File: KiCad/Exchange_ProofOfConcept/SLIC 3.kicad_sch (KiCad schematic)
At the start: 9 parts

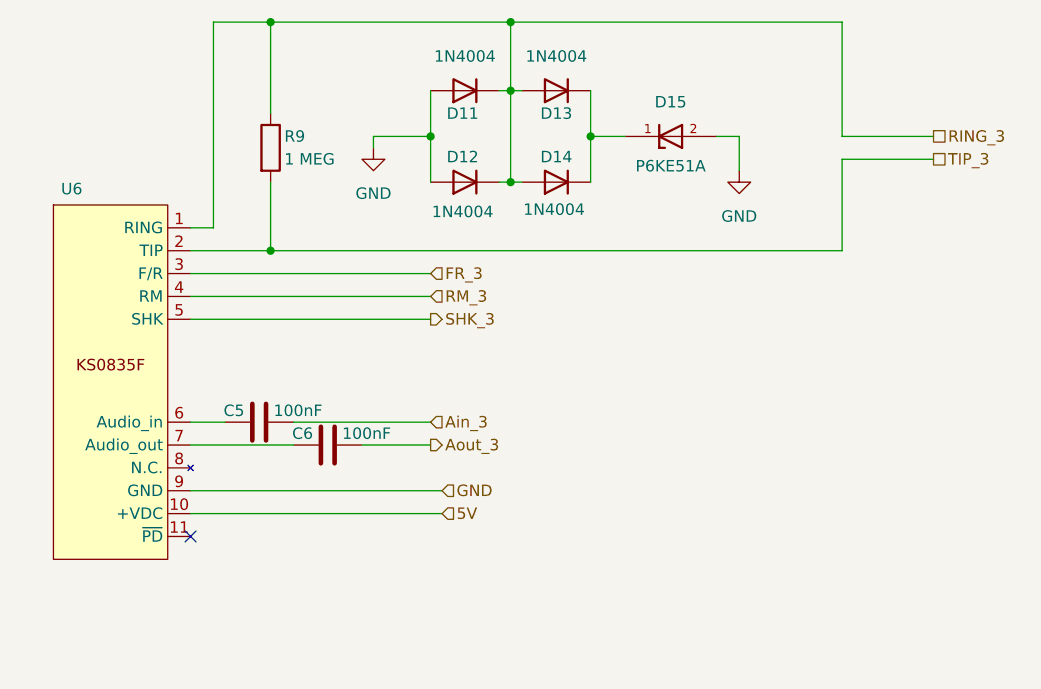
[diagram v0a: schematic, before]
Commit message: deleted:    KiCad/Exchange_ProofOfConcept/Exchange_ProofOfConcept-backups/Exchange_ProofOfConcept-2024-08-28_233227.zip 	deleted:    KiCad/Exchange_ProofOfConcept/Exchange_ProofOfConcept-backups/Exchange_ProofOfConcept-2024-08-28_234504.zip 	deleted:    KiCad/Exchange_ProofOfConcept/Exchange_ProofOfConcept-backups/Exchange_ProofOfConcept-2024-09-04_201626.zip 	deleted:    KiCad/Exchange_ProofOfConcept/Exchange_ProofOfConcept-backups/Exchange_ProofOfConcept-2024-09-04_202659.zip 	deleted:    KiCad/Exchange_ProofOfConcept/Exchange_ProofOfConcept-backups/Exchange_ProofOfConcept-2024-09-04_203703.zip 	deleted:    KiCad/Exchange_ProofOfConcept/Exchange_ProofOfConcept-backups/Exchange_ProofOfConcept-2024-09-04_204710.zip 	deleted:    KiCad/Exchange_ProofOfConcept/Exchange_ProofOfConcept-backups/Exchange_ProofOfConcept-2024-09-04_205754.zip 	deleted:    KiCad/Exchange_ProofOfConcept/Exchange_ProofOfConcept-backups/Exchange_ProofOfConcept-2024-09-05_153643.zip 	deleted:    KiCad/Exchange_ProofOfConcept/Exchange_ProofOfConcept-backups/Exchange_ProofOfConcept-2024-09-05_161017.zip 	deleted:    KiCad/Exchange_ProofOfConcept/Exchange_ProofOfConcept-backups/Exchange_ProofOfConcept-2024-09-05_162441.zip 	deleted:    KiCad/Exchange_ProofOfConcept/Exchange_ProofOfConcept-backups/Exchange_ProofOfConcept-2024-09-05_163641.zip 	deleted:    KiCad/Exchange_ProofOfConcept/Exchange_ProofOfConcept-backups/Exchange_ProofOfConcept-2024-09-06_180233.zip 	deleted:    KiCad/Exchange_ProofOfConcept/Exchange_ProofOfConcept-backups/Exchange_ProofOfConcept-2024-09-06_180943.zip 	deleted:    KiCad/Exchange_ProofOfConcept/Exchange_ProofOfConcept-backups/Exchange_ProofOfConcept-2024-09-06_182256.zip 	deleted:    KiCad/Exchange_ProofOfConcept/Exchange_ProofOfConcept-backups/Exchange_ProofOfConcept-2024-09-06_185314.zip 	deleted:    KiCad/Exchange_ProofOfConcept/Exchange_ProofOfConcept-backups/Exchange_ProofOfConcept-2024-09-06_191143.zip 	deleted:    KiCad/Exchange_ProofOfConcept/Exchange_ProofOfConcep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
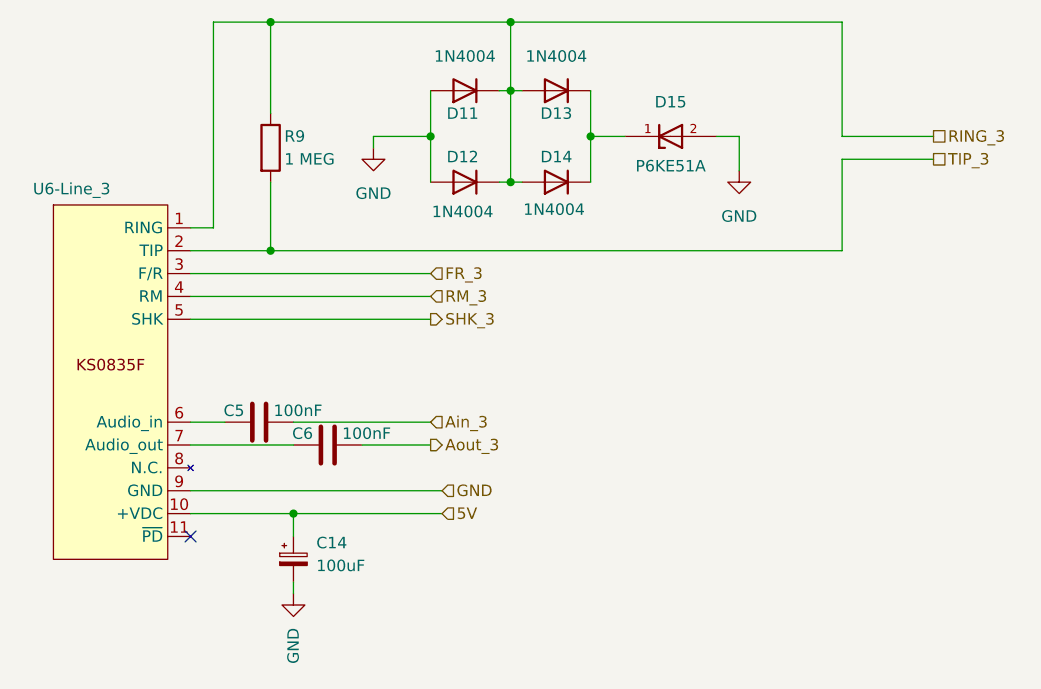
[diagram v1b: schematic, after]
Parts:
- added C14: 100uF, Capacitor_THT:CP_Radial_D5.0mm_P2.00mm, symbol Device:C_Polarized_Small
- renumbered U6 to U6-Line_3
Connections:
- net 5V: now also C14.1
- net GND: now also C14.2
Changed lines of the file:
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@@
+	)
+	(junction
+		(at 63.5 102.87)
+		(diameter 0)
+		(color 0 0 0 0)
 	)
 	(junction
@@
 	(wire
 		(pts
+			(xy 63.5 105.41) (xy 63.5 102.87)
+		)
+		(stroke
+			(width 0)
+			(type default)
+		)
+	)
+	(wire
+		(pts
 			(xy 78.74 60.96) (xy 72.39 60.96)
 		)
@@
 	(wire
 		(pts
-			(xy 52.07 102.87) (xy 80.01 102.87)
+			(xy 63.5 110.49) (xy 63.5 111.76)
+		)
+		(stroke
+			(width 0)
+			(type default)
+		)
+	)
+	(wire
+		(pts
+			(xy 52.07 102.87) (xy 63.5 102.87)
 		)
 		(stroke
@@
 		(pts
 			(xy 60.96 48.26) (xy 60.96 58.42)
+		)
+		(stroke
+			(width 0)
+			(type default)
+		)
+	)
+	(wire
+		(pts
+			(xy 63.5 102.87) (xy 80.01 102.87)
 		)
 		(stroke
@@
 			)
 			(justify left)
+		)
+	)
+	(symbol
+		(lib_id "power:GND")
+		(at 63.5 111.76 0)
+		(unit 1)
+		(exclude_from_sim no)
+		(in_bom yes)
+		(on_board yes)
+		(dnp no)
+		(fields_autoplaced yes)
+		(property "Reference" "#PWR028"
+			(at 63.5 118.11 0)
+			(effects
+				(font
+					(size 1.27 1.27)
+				)
+				(hide yes)
+			)
+		)
+		(property "Value" "GND"
+			(at 63.5001 115.57 90)
+			(effects
+				(font
+					(size 1.27 1.27)
+				)
+				(justify right)
+			)
+		)
+		(property "Footprint" ""
+			(at 63.5 111.76 0)
+			(effects
+				(font
+					(size 1.27 1.27)
+				)
+				(hide yes)
+			)
+		)
+		(property "Datasheet" ""
+			(at 63.5 111.76 0)
+			(effects
+				(font
+					(size 1.27 1.27)
+				)
+				(hide yes)
+			)
+		)
+		(property "Description" "Power symbol creates a global label with name \"GND\" , ground"
+			(at 63.5 111.76 0)
+			(effects
+				(font
+					(size 1.27 1.27)
+				)
+				(hide yes)
+			)
+		)
+		(pin "1"
+		)
+		(instances
+			(project "Exchange_ProofOfConcept"
+				(path "/a3aa82f3-37b8-406c-999a-d11513c8e1fa/040ba3ba-5799-4474-9c9d-b13ff16e9b51"
+					(reference "#PWR028")
+					(unit 1)
+				)
+			)
 		)
 	)
@@
 		(on_board yes)
 		(dnp no)
-		(property "Reference" "U6"
+		(property "Reference" "U6-Line_3"
 			(at 38.862 66.802 0)
 			(effects
@@
 			(project "Exchange_ProofOfConcept"
 				(path "/a3aa82f3-37b8-406c-999a-d11513c8e1fa/040ba3ba-5799-4474-9c9d-b13ff16e9b51"
-					(reference "U6")
+					(reference "U6-Line_3")
 					(unit 1)
 				)
@@
 					(unit 1)
 				)
+			)
+		)
+	)
+	(symbol
+		(lib_id "Device:C_Polarized_Small")
+		(at 63.5 107.95 0)
+		(unit 1)
+		(exclude_from_sim no)
+		(in_bom yes)
+		(on_board yes)
+		(dnp no)
+		(fields_autoplaced yes)
+		(property "Reference" "C14"
+			(at 66.04 106.1338 0)
+			(effects
+				(font
+					(size 1.27 1.27)
+				)
+				(justify left)
+			)
+		)
+		(property "Value" "100uF"
+			(at 66.04 108.6738 0)
+			(effects
+				(font
+					(size 1.27 1.27)
+				)
+				(justify left)
+			)
+		)
+		(property "Footprint" "Capacitor_THT:CP_Radial_D5.0mm_P2.00mm"
+			(at 63.5 107.95 0)
+			(effects
+				(font
+					(size 1.27 1.27)
+				)
+				(hide yes)
+			)
+		)
+		(property "Datasheet" "~"
+			(at 63.5 107.95 0)
+			(effects
+				(font
+					(size 1.27 1.27)
+				)
+				(hide yes)
+			)
+		)
+		(property "Description" "Polarized capacitor, small symbol"
+			(at 63.5 107.95 0)
+			(effects
+				(font
+					(size 1.27 1.27)
+				)
+				(hide yes)
+			)
+		)
+		(pin "1"
+		)
+		(pin "2"
+		)
+		(instances
+			(project "Exchange_ProofOfConcept"
+				(path "/a3aa82f3-37b8-406c-999a-d11513c8e1fa/040ba3ba-5799-4474-9c9d-b13ff16e9b51"
+					(reference "C14")
+					(unit 1)
+				)

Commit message: new file:   KiCad/Exchange_ProofOfConcept/ESP-Unit/ESP-Unit-backups/ESP-Unit-2024-10-22_204833.zip 	new file:   KiCad/Exchange_ProofOfConcept/ESP-Unit/ESP-Unit-backups/ESP-Unit-2024-10-22_205851.zip 	new file:   KiCad/Exchange_ProofOfConcept/ESP-Unit/ESP-Unit-backups/ESP-Unit-2024-10-22_214835.zip 	new file:   KiCad/Exchange_ProofOfConcept/ESP-Unit/ESP-Unit-backups/ESP-Unit-2024-10-31_190638.zip 	new file:   KiCad/Exchange_ProofOfConcept/ESP-Unit/ESP-Unit.kicad_pcb 	new file:   KiCad/Exchange_ProofOfConcept/ESP-Unit/ESP-Unit.kicad_prl 	new file:   KiCad/Exchange_ProofOfConcept/ESP-Unit/ESP-Unit.kicad_pro 	new file:   KiCad/Exchange_ProofOfConcept/ESP-Unit/ESP-Unit.kicad_sch 	new file:   KiCad/Exchange_ProofOfConcept/ESP-Unit/fp-info-cache 	deleted:    KiCad/Exchange_ProofOfConcept/Exchange_ProofOfConcept-backups/Exchange_ProofOfConcept-2024-09-09_193050.zip 	deleted:    KiCad/Exchange_ProofOfConcept/Exchange_ProofOfConcept-backups/Exchange_ProofOfConcept-2024-09-10_220108.zip 	deleted:    KiCad/Exchange_ProofOfConcept/Exchange_ProofOfConcept-backups/Exchange_ProofOfConcept-2024-09-10_232037.zip 	deleted:    KiCad/Exchange_ProofOfConcept/Exchange_ProofOfConcept-backups/Exchange_ProofOfConcept-2024-09-11_034329.zip 	deleted:    KiCad/Exchange_ProofOfConcept/Exchange_ProofOfConcept-backups/Exchange_ProofOfConcept-2024-09-11_195456.zip 	deleted:    KiCad/Exchange_ProofOfConcept/Exchange_ProofOfConcept-backups/Exchange_ProofOfConcept-2024-09-17_174014.zip 	deleted:    KiCad/Exchange_ProofOfConcept/Exchange_ProofOfConcept-backups/Exchange_ProofOfConcept-2024-09-17_181112.zip 	deleted:    KiCad/Exchange_ProofOfConcept/Exchange_ProofOfConcept-backups/Exchange_ProofOfConcept-2024-09-19_202603.zip 	deleted:    KiCad/Exchange_ProofOfConcept/Exchange_ProofOfConcept-backups/Exchange_ProofOfConcept-2024-09-19_204637.zip 	deleted:    KiCad/Exchange_ProofOfConcept/Exchange_ProofOfConcept-backups/Exchange_ProofOfConcept-2024-09-19_205646.zip 	deleted:    KiCad/Exchange_ProofOfConcep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
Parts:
- R9: footprint Resistor_THT:R_Axial_DIN0204_L3.6mm_D1.6mm_P5.08mm_Horizontal -> Resistor_THT:R_Axial_DIN0207_L6.3mm_D2.5mm_P7.62mm_Horizontal
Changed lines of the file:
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@@
 			)
 		)
-		(property "Footprint" "Resistor_THT:R_Axial_DIN0204_L3.6mm_D1.6mm_P5.08mm_Horizontal"
+		(property "Footprint" "Resistor_THT:R_Axial_DIN0207_L6.3mm_D2.5mm_P7.62mm_Horizontal"
 			(at 59.182 62.23 90)
 			(effects

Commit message: deleted:    KiCad/Exchange_ProofOfConcept/Exchange_ProofOfConcept-backups/Exchange_ProofOfConcept-2024-09-22_005800.zip 	deleted:    KiCad/Exchange_ProofOfConcept/Exchange_ProofOfConcept-backups/Exchange_ProofOfConcept-2024-09-22_010415.zip 	deleted:    KiCad/Exchange_ProofOfConcept/Exchange_ProofOfConcept-backups/Exchange_ProofOfConcept-2024-09-22_093037.zip 	deleted:    KiCad/Exchange_ProofOfConcept/Exchange_ProofOfConcept-backups/Exchange_ProofOfConcept-2024-09-22_093847.zip 	deleted:    KiCad/Exchange_ProofOfConcept/Exchange_ProofOfConcept-backups/Exchange_ProofOfConcept-2024-09-22_094927.zip 	deleted:    KiCad/Exchange_ProofOfConcept/Exchange_ProofOfConcept-backups/Exchange_ProofOfConcept-2024-10-02_184119.zip 	deleted:    KiCad/Exchange_ProofOfConcept/Exchange_ProofOfConcept-backups/Exchange_ProofOfConcept-2024-10-06_223658.zip 	new file:   KiCad/Exchange_ProofOfConcept/Exchange_ProofOfConcept-backups/Exchange_ProofOfConcept-2024-11-20_223020.zip 	new file:   KiCad/Exchange_ProofOfConcept/Exchange_ProofOfConcept-backups/Exchange_ProofOfConcept-2024-11-20_223933.zip 	new file:   KiCad/Exchange_ProofOfConcept/Exchange_ProofOfConcept-backups/Exchange_ProofOfConcept-2024-11-20_224852.zip 	new file:   KiCad/Exchange_ProofOfConcept/Exchange_ProofOfConcept-backups/Exchange_ProofOfConcept-2024-11-20_230009.zip 	new file:   KiCad/Exchange_ProofOfConcept/Exchange_ProofOfConcept-backups/Exchange_ProofOfConcept-2024-11-20_231023.zip 	new file:   KiCad/Exchange_ProofOfConcept/Exchange_ProofOfConcept-backups/Exchange_ProofOfConcept-2024-11-20_231736.zip 	modified:   KiCad/Exchange_ProofOfConcept/Exchange_ProofOfConcept.kicad_pcb 	modified:   KiCad/Exchange_ProofOfConcept/Exchange_ProofOfConcept.kicad_prl 	modified:   KiCad/Exchange_ProofOfConcept/Exchange_ProofOfConcept.kicad_pro 	modified:   KiCad/Exchange_ProofOfConcept/Exchange_ProofOfConcept.kicad_sch 	modified:   KiCad/Exchange_ProofOfConcept/SLIC 1.kicad_sch 	modified:   KiCad/Exchange_ProofOfConcept/SLIC 1_sch.kicad_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
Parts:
- R9: footprint Resistor_THT:R_Axial_DIN0207_L6.3mm_D2.5mm_P7.62mm_Horizontal -> Resistor_THT:R_Axial_DIN0207_L6.3mm_D2.5mm_P2.54mm_Vertical
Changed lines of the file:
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@@
 			)
 		)
-		(property "Footprint" "Resistor_THT:R_Axial_DIN0207_L6.3mm_D2.5mm_P7.62mm_Horizontal"
+		(property "Footprint" "Resistor_THT:R_Axial_DIN0207_L6.3mm_D2.5mm_P2.54mm_Vertical"
 			(at 59.182 62.23 90)
 			(effects
